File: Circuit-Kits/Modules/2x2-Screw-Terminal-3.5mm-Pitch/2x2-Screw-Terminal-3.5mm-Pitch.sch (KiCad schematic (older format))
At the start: 0 parts

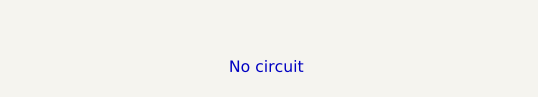
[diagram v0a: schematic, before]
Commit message: Screw terminal layout.
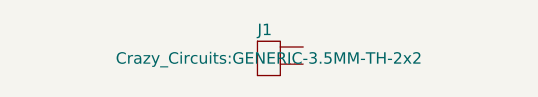
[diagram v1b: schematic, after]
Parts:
- added J1: Conn_2, Crazy_Circuits:GENERIC-3.5MM-TH-2x2, symbol Conn_2
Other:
- note removed: "No circuit"
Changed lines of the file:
@@
 EESchema Schematic File Version 2
 LIBS:crazy_circuits
+LIBS:2x2-Screw-Terminal-3.5mm-Pitch-cache
 EELAYER 25 0
 EELAYER END
@@
 Comment4 ""
 $EndDescr
-Text Notes 4775 3650 0    50   ~ 0
-No circuit
+$Comp
+L Conn_2 J1
+U 1 1 587EB9D9
+P 4950 3575
+F 0 "J1" H 4900 3700 50  0000 L CNN
+F 1 "Conn_2" H 4900 3450 50  0001 L CNN
+F 2 "Crazy_Circuits:GENERIC-3.5MM-TH-2x2" H 4950 3575 50  0000 C CNN
+F 3 "" H 4950 3575 50  0000 C CNN
+F 4 "OnShore" H 4950 3575 60  0001 C CNN "MF_Name"
+F 5 "OSTTE020104" H 4950 3575 60  0001 C CNN "MF_PN"
+F 6 "Digikey" H 4950 3575 60  0001 C CNN "S1_Name"
+F 7 "ED2740-ND" H 4950 3575 60  0001 C CNN "S1_PN"
+F 8 "SCREW TERMINAL 3.5MM PITCH 1x2" H 4950 3575 60  0001 C CNN "Description"
+	1    4950 3575
+	1    0    0    -1
+$EndComp
 $EndSCHEMATC

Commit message: Added 2x2 screw terminal 3.5mm pitch.
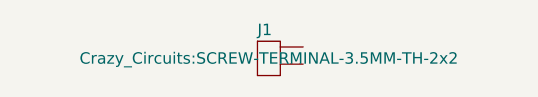
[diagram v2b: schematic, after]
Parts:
- J1: footprint Crazy_Circuits:GENERIC-3.5MM-TH-2x2 -> Crazy_Circuits:SCREW-TERMINAL-3.5MM-TH-2x2
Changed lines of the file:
@@
 F 0 "J1" H 4900 3700 50  0000 L CNN
 F 1 "Conn_2" H 4900 3450 50  0001 L CNN
-F 2 "Crazy_Circuits:GENERIC-3.5MM-TH-2x2" H 4950 3575 50  0000 C CNN
+F 2 "Crazy_Circuits:SCREW-TERMINAL-3.5MM-TH-2x2" H 4950 3575 50  0000 C CNN
 F 3 "" H 4950 3575 50  0000 C CNN
 F 4 "OnShore" H 4950 3575 60  0001 C CNN "MF_Name"
